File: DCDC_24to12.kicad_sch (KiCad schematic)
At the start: 16 parts, among them J4 Power_IN, U1 BD9F800MUX-ZE2

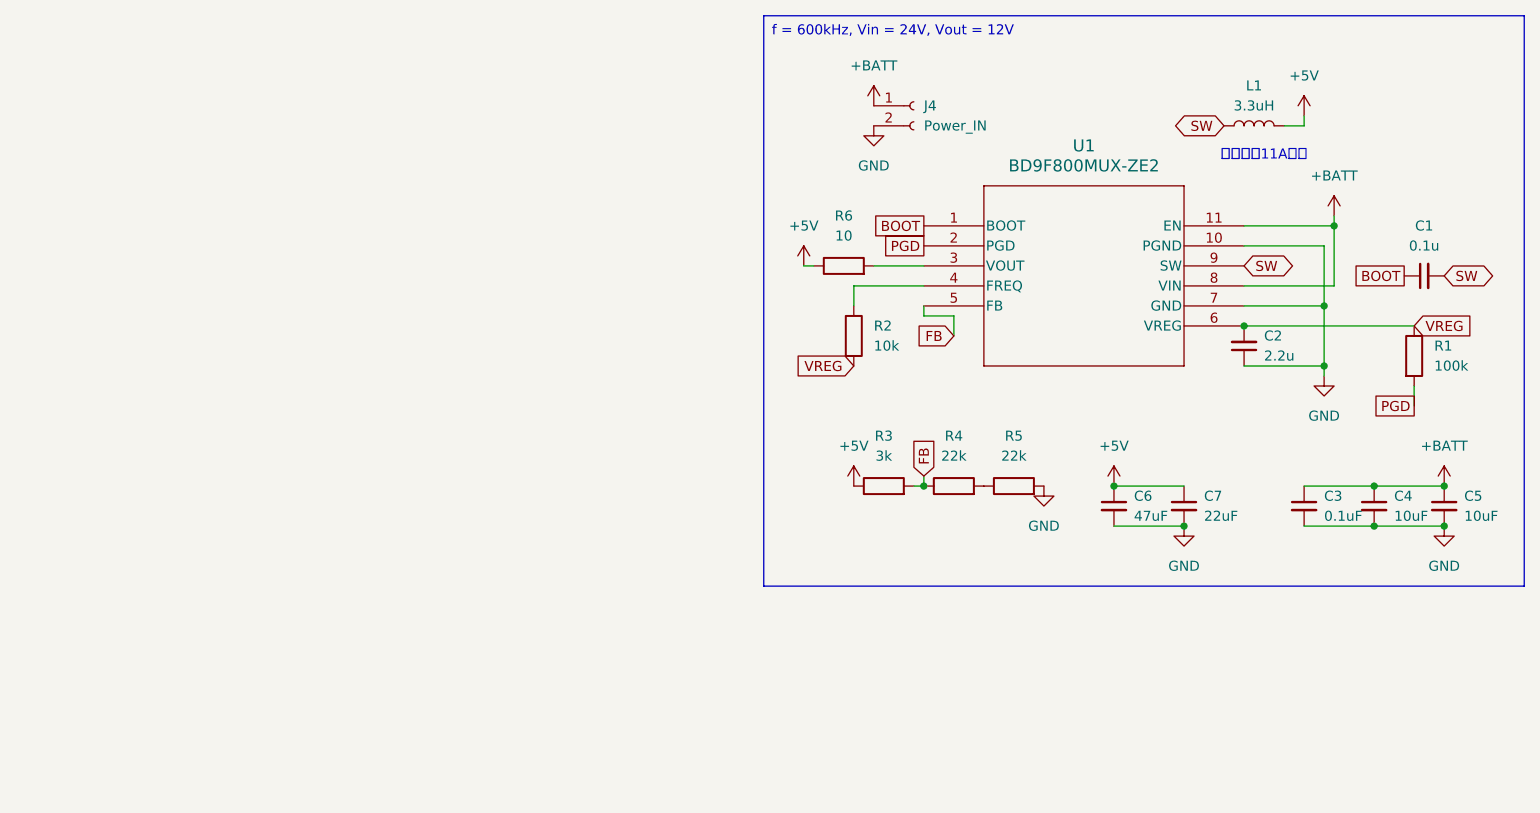
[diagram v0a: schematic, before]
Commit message: 抵抗値とか修正
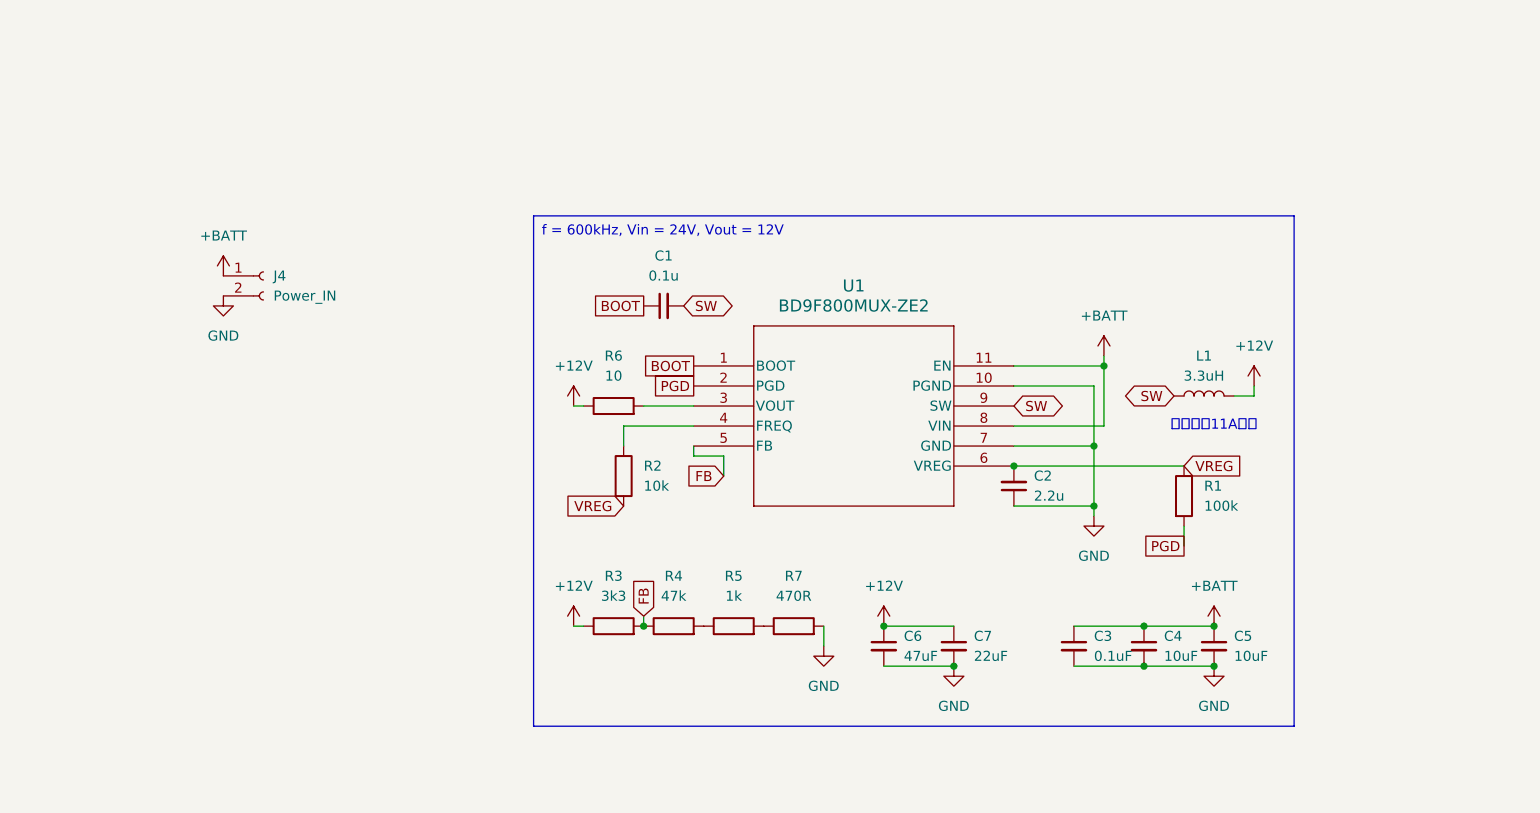
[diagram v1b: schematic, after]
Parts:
- added R7: 470R, symbol Device:R
- R3: value 3k -> 3k3
- R4: value 22k -> 47k
- R5: value 22k -> 1k
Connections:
- net GND: now also R7.2; no longer R5.2
- net +5V renamed +12V
- new net: R5.2, R7.1
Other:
- moved on the sheet: C1, C2, C3, C4, C5, C6, C7, J4, L1, R1, R2, R3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

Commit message: LED追加したり
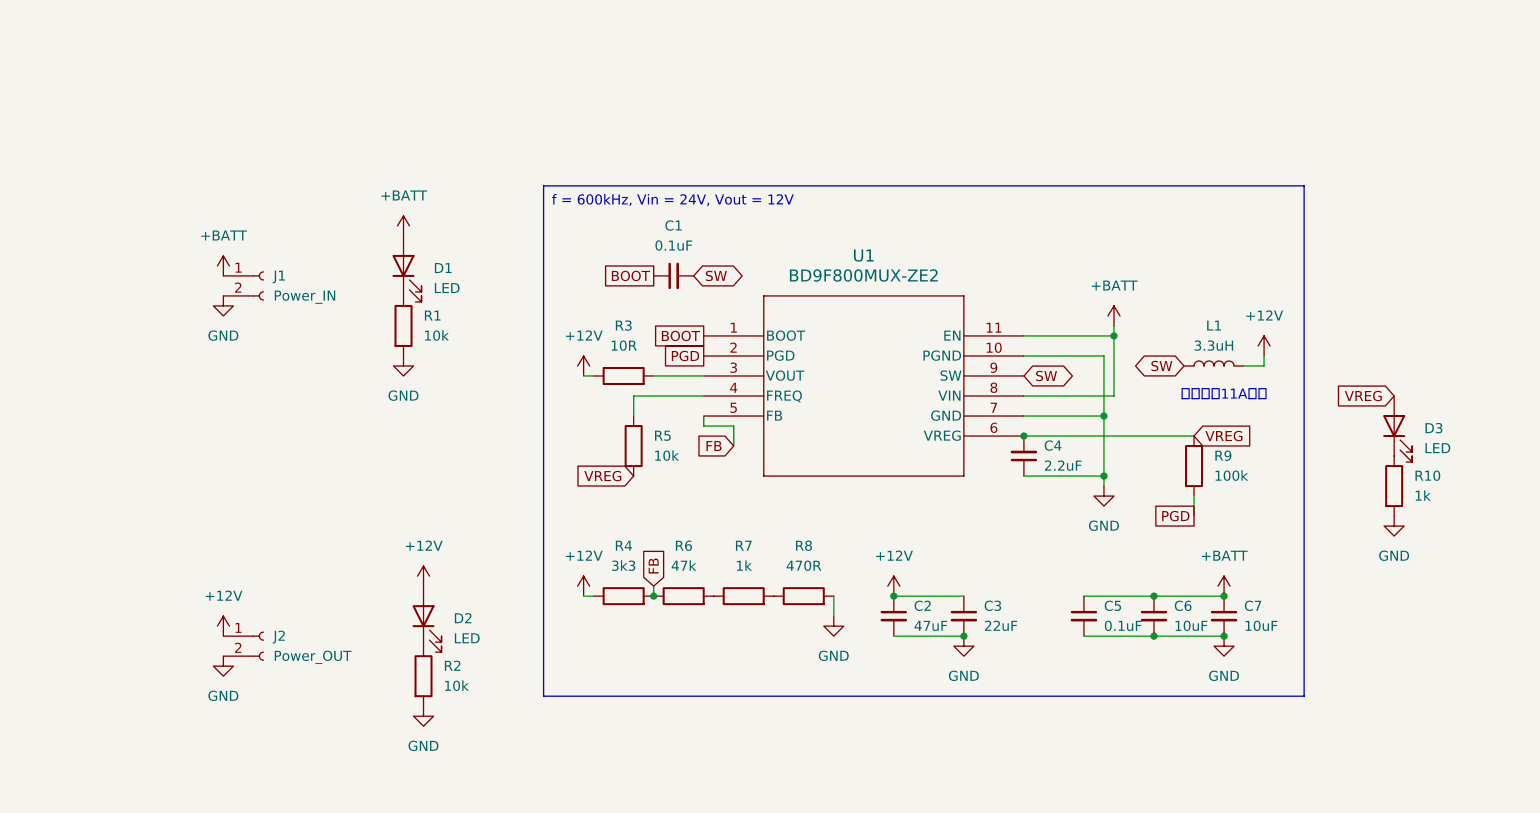
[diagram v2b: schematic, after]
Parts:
- added D1, D2, D3: LED, LED_SMD:LED_0603_1608Metric, symbol Device:LED
- added J2: Power_OUT, Connector_AMASS:AMASS_XT60-F_1x02_P7.20mm_Vertical, symbol Connector:Conn_01x02_Socket
- added R1, R2: 10k, Resistor_SMD:R_0805_2012Metric, symbol Device:R
- added R10: 1k, Resistor_SMD:R_0805_2012Metric, symbol Device:R
- C1: value 0.1u -> 0.1uF; footprint (none) -> Capacitor_SMD:C_0805_2012Metric
- C2: renamed from C6; footprint (none) -> Capacitor_SMD:C_1206_3216Metric
- C3: renamed from C7; footprint (none) -> Capacitor_SMD:C_0805_2012Metric
- C4: renamed from C2; value 2.2u -> 2.2uF
- C5: renamed from C3; footprint (none) -> Capacitor_SMD:C_0805_2012Metric
- C6: renamed from C4; footprint (none) -> Capacitor_SMD:C_0805_2012Metric
- C7: renamed from C5; footprint (none) -> Capacitor_SMD:C_0805_2012Metric
- J1: renamed from J4; footprint (none) -> Connector_AMASS:AMASS_XT60-M_1x02_P7.20mm_Vertical
- R3: renamed from R6; value 10 -> 10R; footprint (none) -> Resistor_SMD:R_0805_2012Metric
- R4: renamed from R3; footprint (none) -> Resistor_SMD:R_0805_2012Metric
- R5: renamed from R2; footprint (none) -> Resistor_SMD:R_0805_2012Metric
- R6: renamed from R4; footprint (none) -> Resistor_SMD:R_0805_2012Metric
- R7: renamed from R5; footprint (none) -> Resistor_SMD:R_0805_2012Metric
- R8: renamed from R7; footprint (none) -> Resistor_SMD:R_0805_2012Metric
- R9: renamed from R1; footprint (none) -> Resistor_SMD:R_0805_2012Metric
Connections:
- net +12V: now also D2.2 (A), J2.1 (Pin_1)
- net +BATT: now also D1.2 (A)
- net GND: now also J2.2 (Pin_2), R1.2, R10.2, R2.2
- net VREG: now also D3.2 (A)
- new net: D2.1 (K), R2.1
- new net: D1.1 (K), R1.1
- new net: D3.1 (K), R10.1
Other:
- moved on the sheet: C1, C2, C3, C4, C5, C6, C7, L1, R3, R4, R5, R6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

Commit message: PGOODを+BATTで吊った
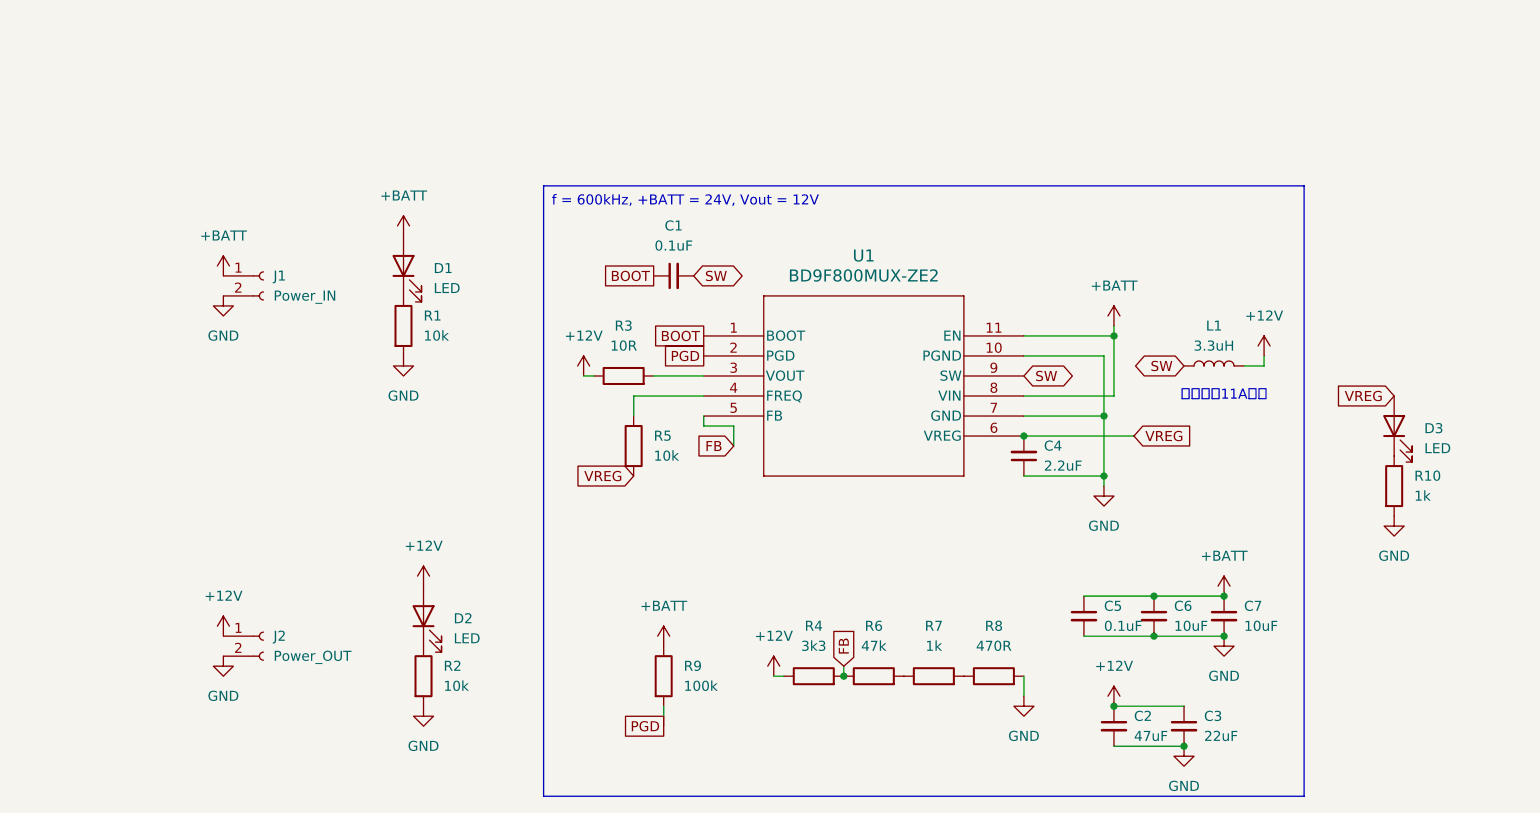
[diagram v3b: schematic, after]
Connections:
- net +BATT: now also R9.1
- net VREG: no longer R9.1
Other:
- moved on the sheet: C2, C3, R4, R6, R7, R8, R9

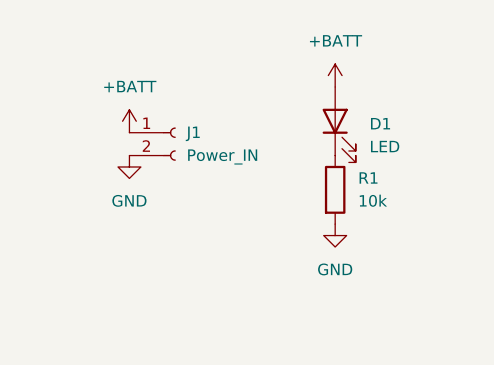
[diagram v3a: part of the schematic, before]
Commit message: 逆接防止ショットキーバリアダイオード
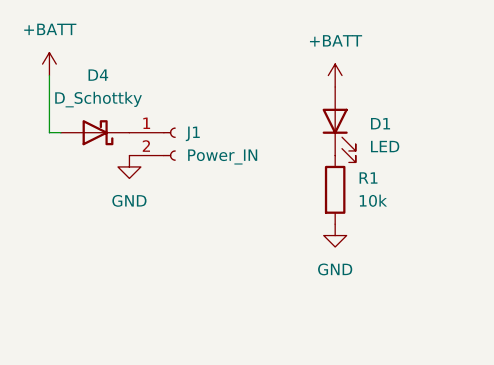
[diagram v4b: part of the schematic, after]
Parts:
- added D4: D_Schottky, symbol Device:D_Schottky
- L1: footprint (none) -> Library:SRP1245A
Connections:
- net +BATT: now also D4.2 (A); no longer J1.1 (Pin_1)
- new net: D4.1 (K), J1.1 (Pin_1)
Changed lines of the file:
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@@
+	(wire
+		(pts
+			(xy 36.83 72.39) (xy 36.83 78.74)
+		)
+		(stroke
+			(width 0)
+			(type default)
+		)
+	)
 	(wire
 		(pts
@@
 		(pts
 			(xy 158.75 133.35) (xy 167.64 133.35)
+		)
+		(stroke
+			(width 0)
+			(type default)
+		)
+	)
+	(wire
+		(pts
+			(xy 36.83 78.74) (xy 38.1 78.74)
 		)
 		(stroke
@@
 	(symbol
 		(lib_id "power:+BATT")
-		(at 45.72 78.74 0)
+		(at 36.83 72.39 0)
 		(unit 1)
 		(exclude_from_sim no)
@@
 		(fields_autoplaced yes)
 		(property "Reference" "#PWR01"
-			(at 45.72 82.55 0)
+			(at 36.83 76.2 0)
 			(effects
 				(font
@@
 		)
 		(property "Value" "+BATT"
-			(at 45.72 73.66 0)
+			(at 36.83 67.31 0)
 			(effects
 				(font
@@
 		)
 		(property "Footprint" ""
-			(at 45.72 78.74 0)
+			(at 36.83 72.39 0)
 			(effects
 				(font
@@
 		)
 		(property "Datasheet" ""
-			(at 45.72 78.74 0)
+			(at 36.83 72.39 0)
 			(effects
 				(font
@@
 		)
 		(property "Description" "Power symbol creates a global label with name \"+BATT\""
-			(at 45.72 78.74 0)
+			(at 36.83 72.39 0)
 			(effects
 				(font
@@
 			)
 		)
-		(property "Footprint" ""
+		(property "Footprint" "Library:SRP1245A"
 			(at 171.45 90.17 0)
 			(effects
@@
 					(unit 1)
 				)
+			)
+		)
+	)
+	(symbol
+		(lib_id "Device:D_Schottky")
+		(at 41.91 78.74 180)
+		(unit 1)
+		(exclude_from_sim no)
+		(in_bom yes)
+		(on_board yes)
+		(dnp no)
+		(fields_autoplaced yes)
+		(property "Reference" "D4"
+			(at 42.2275 72.39 0)
+			(effects
+				(font
+					(size 1.27 1.27)
+				)
+			)
+		)
+		(property "Value" "D_Schottky"
+			(at 42.2275 74.93 0)
+			(effects
+				(font
+					(size 1.27 1.27)
+				)
+			)
+		)
+		(property "Footprint" ""
+			(at 41.91 78.74 0)
+			(effects
+				(font
+					(size 1.27 1.27)
+				)
+				(hide yes)
+			)
+		)
+		(property "Datasheet" "~"
+			(at 41.91 78.74 0)
+			(effects
+				(font
+					(size 1.27 1.27)
+				)
+				(hide yes)
+			)
+		)
+		(property "Description" "Schottky diode"
+			(at 41.91 78.74 0)
+			(effects
+				(font
+					(size 1.27 1.27)
+				)
+				(hide yes)
+			)
+		)
+		(pin "2"
+		)
+		(pin "1"
+		)
+		(instances
+			(project ""
+				(path "/9b31bb12-b0a4-46c2-8fe3-73cecf9f3124"
+					(reference "D4")
+					(unit 1)
+				)

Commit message: C_VREG選定完了
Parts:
- C4: footprint (none) -> Capacitor_SMD:C_0805_2012Metric
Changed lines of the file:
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@@
 			)
 		)
-		(property "Footprint" ""
+		(property "Footprint" "Capacitor_SMD:C_0805_2012Metric"
 			(at 147.32 101.6 0)
 			(effects

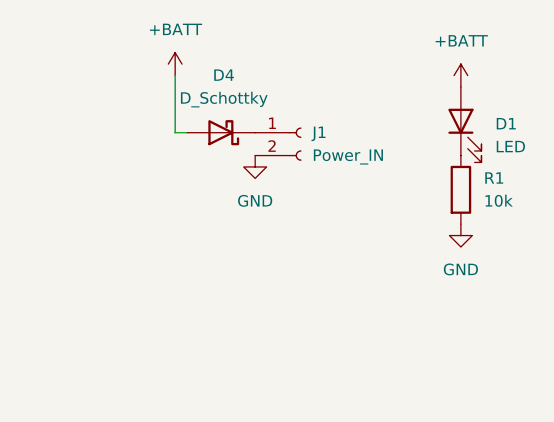
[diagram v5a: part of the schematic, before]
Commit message: 逆接保護回路変更 損失抑えver.
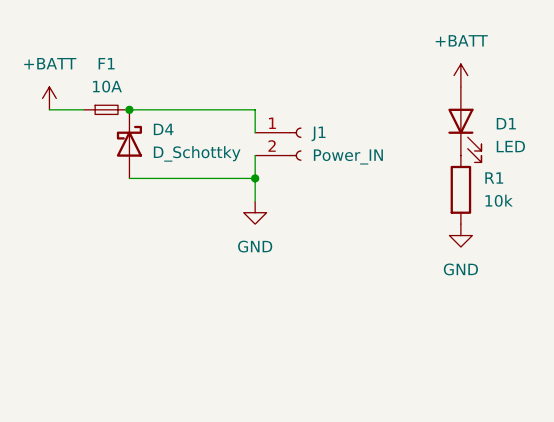
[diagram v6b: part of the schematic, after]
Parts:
- added F1: 10A, symbol Device:Fuse_Small
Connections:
- net +BATT: now also F1.1; no longer D4.2 (A)
- net GND: now also D4.2 (A)
- net at D4.1 (K), J1.1 (Pin_1): now also F1.2
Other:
- moved on the sheet: D4
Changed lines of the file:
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@@
 	)
 	(junction
+		(at 31.75 76.2)
+		(diameter 0)
+		(color 0 0 0 0)
+	)
+	(junction
 		(at 157.48 96.52)
 		(diameter 0)
@@
 	)
 	(junction
+		(at 45.72 83.82)
+		(diameter 0)
+		(color 0 0 0 0)
+	)
+	(junction
 		(at 163.83 119.38)
 		(diameter 0)
@@
 	(wire
 		(pts
-			(xy 36.83 72.39) (xy 36.83 78.74)
-		)
-		(stroke
-			(width 0)
-			(type default)
-		)
-	)
-	(wire
-		(pts
 			(xy 158.75 86.36) (xy 158.75 93.98)
 		)
@@
 	(wire
 		(pts
+			(xy 22.86 76.2) (xy 26.67 76.2)
+		)
+		(stroke
+			(width 0)
+			(type default)
+		)
+	)
+	(wire
+		(pts
 			(xy 91.44 91.44) (xy 92.71 91.44)
 		)
@@
 	(wire
 		(pts
+			(xy 31.75 83.82) (xy 45.72 83.82)
+		)
+		(stroke
+			(width 0)
+			(type default)
+		)
+	)
+	(wire
+		(pts
+			(xy 45.72 76.2) (xy 31.75 76.2)
+		)
+		(stroke
+			(width 0)
+			(type default)
+		)
+	)
+	(wire
+		(pts
 			(xy 147.32 88.9) (xy 157.48 88.9)
 		)
@@
 	(wire
 		(pts
+			(xy 45.72 86.36) (xy 45.72 83.82)
+		)
+		(stroke
+			(width 0)
+			(type default)
+		)
+	)
+	(wire
+		(pts
 			(xy 147.32 86.36) (xy 158.75 86.36)
 		)
@@
 	(wire
 		(pts
-			(xy 158.75 133.35) (xy 167.64 133.35)
+			(xy 45.72 78.74) (xy 45.72 76.2)
+		)
+		(stroke
+			(width 0)
+			(type default)
+		)
+	)
+	(wire
+		(pts
+			(xy 45.72 83.82) (xy 45.72 81.28)
 		)
 		(stroke
@@
 	(wire
 		(pts
-			(xy 36.83 78.74) (xy 38.1 78.74)
+			(xy 158.75 133.35) (xy 167.64 133.35)
 		)
 		(stroke
@@
 	(symbol
 		(lib_id "power:+BATT")
-		(at 36.83 72.39 0)
+		(at 22.86 76.2 0)
 		(unit 1)
 		(exclude_from_sim no)
@@
 		(fields_autoplaced yes)
 		(property "Reference" "#PWR01"
-			(at 36.83 76.2 0)
+			(at 22.86 80.01 0)
 			(effects
 				(font
@@
 		)
 		(property "Value" "+BATT"
-			(at 36.83 67.31 0)
+			(at 22.86 71.12 0)
 			(effects
 				(font
@@
 		)
 		(property "Footprint" ""
-			(at 36.83 72.39 0)
+			(at 22.86 76.2 0)
 			(effects
 				(font
@@
 		)
 		(property "Datasheet" ""
-			(at 36.83 72.39 0)
+			(at 22.86 76.2 0)
 			(effects
 				(font
@@
 		)
 		(property "Description" "Power symbol creates a global label with name \"+BATT\""
-			(at 36.83 72.39 0)
+			(at 22.86 76.2 0)
 			(effects
 				(font
@@
 	(symbol
 		(lib_id "power:GND")
-		(at 45.72 81.28 0)
+		(at 45.72 86.36 0)
 		(unit 1)
 		(exclude_from_sim no)
@@
 		(fields_autoplaced yes)
 		(property "Reference" "#PWR02"
-			(at 45.72 87.63 0)
+			(at 45.72 92.71 0)
 			(effects
 				(font
@@
 		)
 		(property "Value" "GND"
-			(at 45.72 86.36 0)
+			(at 45.72 91.44 0)
 			(effects
 				(font
@@
 		)
 		(property "Footprint" ""
-			(at 45.72 81.28 0)
+			(at 45.72 86.36 0)
 			(effects
 				(font
@@
 		)
 		(property "Datasheet" ""
-			(at 45.72 81.28 0)
+			(at 45.72 86.36 0)
 			(effects
 				(font
@@
 		)
 		(property "Description" "Power symbol creates a global label with name \"GND\" , ground"
-			(at 45.72 81.28 0)
+			(at 45.72 86.36 0)
 			(effects
 				(font
@@
 	(symbol
 		(lib_id "Device:D_Schottky")
-		(at 41.91 78.74 180)
+		(at 31.75 80.01 270)
 		(unit 1)
 		(exclude_from_sim no)
@@
 		(fields_autoplaced yes)
 		(property "Reference" "D4"
-			(at 42.2275 72.39 0)
+			(at 34.29 78.4224 90)
 			(effects
 				(font
 					(size 1.27 1.27)
 				)
+				(justify left)
 			)
 		)
 		(property "Value" "D_Schottky"
-			(at 42.2275 74.93 0)
+			(at 34.29 80.9624 90)
 			(effects
 				(font
 					(size 1.27 1.27)
 				)
+				(justify left)
 			)
 		)
 		(property "Footprint" ""
-			(at 41.91 78.74 0)
+			(at 31.75 80.01 0)
 			(effects
 				(font
@@
 		)
 		(property "Datasheet" "~"
-			(at 41.91 78.74 0)
+			(at 31.75 80.01 0)
 			(effects
 				(font
@@
 		)
 		(property "Description" "Schottky diode"
-			(at 41.91 78.74 0)
+			(at 31.75 80.01 0)
 			(effects
 				(font
@@
 					(unit 1)
 				)
+			)
+		)
+	)
+	(symbol
+		(lib_id "Device:Fuse_Small")
+		(at 29.21 76.2 0)
+		(unit 1)
+		(exclude_from_sim no)
+		(in_bom yes)
+		(on_board yes)
+		(dnp no)
+		(fields_autoplaced yes)
+		(property "Reference" "F1"
+			(at 29.21 71.12 0)
+			(effects
+				(font
+					(size 1.27 1.27)
+				)
+			)
+		)
+		(property "Value" "10A"
+			(at 29.21 73.66 0)
+			(effects
+				(font
+					(size 1.27 1.27)
+				)
+			)
+		)
+		(property "Footprint" ""
+			(at 29.21 76.2 0)
+			(effects
+				(font
+					(size 1.27 1.27)
+				)
+				(hide yes)
+			)
+		)
+		(property "Datasheet" "~"
+			(at 29.21 76.2 0)
+			(effects
+				(font
+					(size 1.27 1.27)
+				)
+				(hide yes)
+			)
+		)
+		(property "Description" "Fuse, small symbol"
+			(at 29.21 76.2 0)
+			(effects
+				(font
+					(size 1.27 1.27)
+				)
+				(hide yes)
+			)
+		)
+		(pin "2"
+		)
+		(pin "1"
+		)
+		(instances
+			(project ""
+				(path "/9b31bb12-b0a4-46c2-8fe3-73cecf9f3124"
+					(reference "F1")
+					(unit 1)
+				)

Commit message: ヒューズ追加
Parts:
- F1: footprint (none) -> FUSE_3557:FUSE_3557-2
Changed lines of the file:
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@@
 			)
 		)
-		(property "Footprint" ""
+		(property "Footprint" "FUSE_3557:FUSE_3557-2"
 			(at 29.21 76.2 0)
 			(effects

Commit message: SBDフットプリント割り当て、PCB更新
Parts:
- D4: footprint (none) -> Diode_SMD:D_SOD-123F
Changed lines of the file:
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@@
 			)
 		)
-		(property "Footprint" ""
+		(property "Footprint" "Diode_SMD:D_SOD-123F"
 			(at 31.75 80.01 0)
 			(effects
